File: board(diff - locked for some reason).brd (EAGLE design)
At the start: 161 x 100 mm, 19 parts, among them IC1 ATMEGA644-20PU, Q1 2N3906, T1 2N3904, T2 2N3904, T3 2N3904, T4 2N3904, U1 MCP1825S-3302E/DB

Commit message: modified board slightly
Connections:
- net GND: now also U1.2, U1.4
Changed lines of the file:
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@@
 <?xml version="1.0" encoding="utf-8"?>
 <!DOCTYPE eagle SYSTEM "eagle.dtd">
-<eagle version="8.4.0">
+<eagle version="8.4.1">
 <drawing>
 <settings>
@@
 <param name="dpMaxLengthDifference" value="10mm"/>
 <param name="dpGapFactor" value="2.5"/>
+<param name="checkAngle" value="0"/>
 <param name="checkFont" value="1"/>
 <param name="checkRestrict" value="1"/>
@@
 <contactref element="C2" pad="-"/>
 <contactref element="C1" pad="-"/>
-<wire x1="11.43" y1="12.05" x2="11.43" y2="20.94" width="0" layer="19" extent="1-1"/>
-<wire x1="29.75" y1="11.44" x2="11.43" y2="20.94" width="0" layer="19" extent="1-1"/>
-<wire x1="27.94" y1="80.01" x2="29.75" y2="11.44" width="0" layer="19" extent="1-1"/>
-<wire x1="16.51" y1="92.71" x2="29.75" y2="11.44" width="0" layer="19" extent="1-1"/>
+<contactref element="U1" pad="2"/>
+<contactref element="U1" pad="4"/>
+<wire x1="61.7996" y1="87" x2="68.2004" y2="87" width="0" layer="19" extent="1-1"/>
+<wire x1="27.94" y1="80.01" x2="61.7996" y2="87" width="0" layer="19" extent="1-1"/>
+<wire x1="16.51" y1="92.71" x2="27.94" y2="80.01" width="0" layer="19" extent="1-1"/>
 <wire x1="17.78" y1="62.23" x2="27.94" y2="80.01" width="0" layer="19" extent="1-1"/>
 <wire x1="17.78" y1="53.34" x2="17.78" y2="62.23" width="0" layer="19" extent="1-1"/>
 <wire x1="17.78" y1="44.45" x2="17.78" y2="53.34" width="0" layer="19" extent="1-1"/>
 <wire x1="17.78" y1="35.56" x2="17.78" y2="44.45" width="0" layer="19" extent="1-1"/>
+<wire x1="11.43" y1="20.94" x2="17.78" y2="35.56" width="0" layer="19" extent="1-1"/>
+<wire x1="11.43" y1="12.05" x2="11.43" y2="20.94" width="0" layer="19" extent="1-1"/>
+<wire x1="29.75" y1="11.44" x2="11.43" y2="12.05" width="0" layer="19" extent="1-1"/>
 </signal>
 <signal name="VCC">

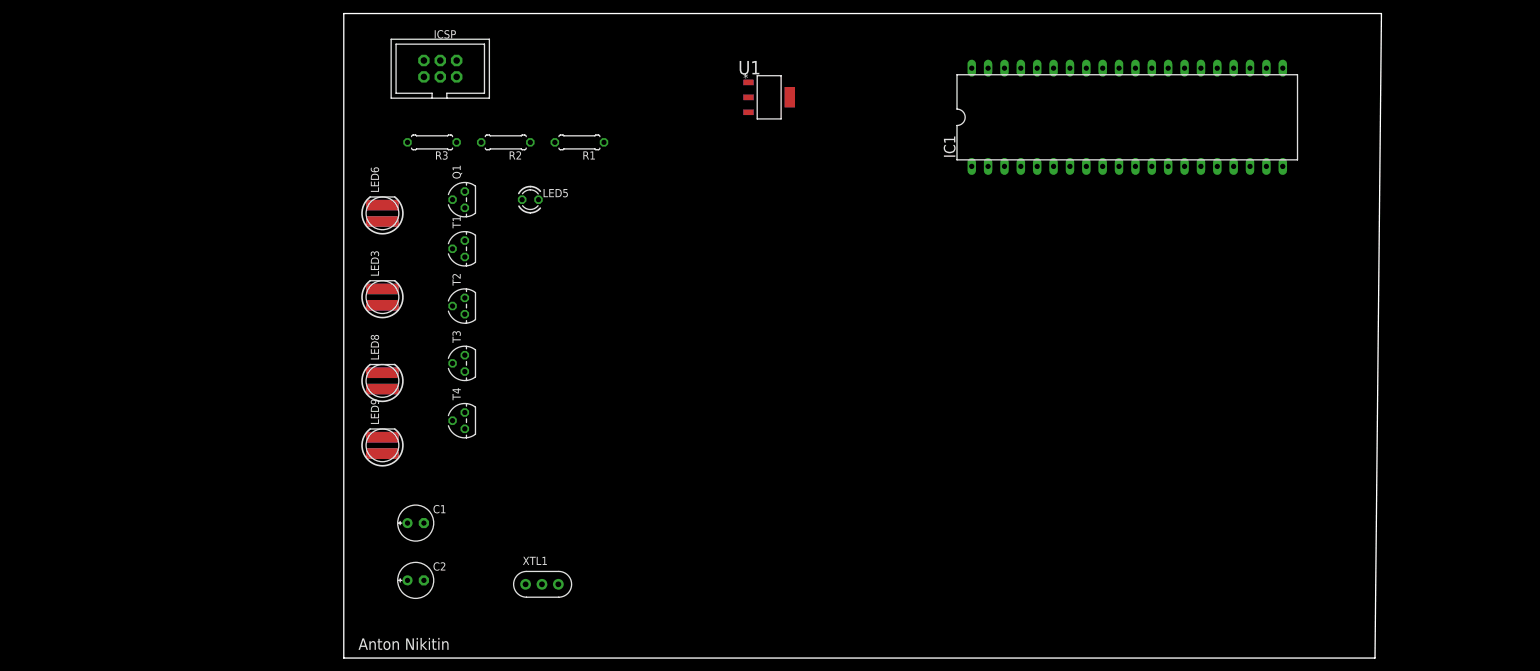
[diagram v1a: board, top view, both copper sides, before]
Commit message: added battery holders
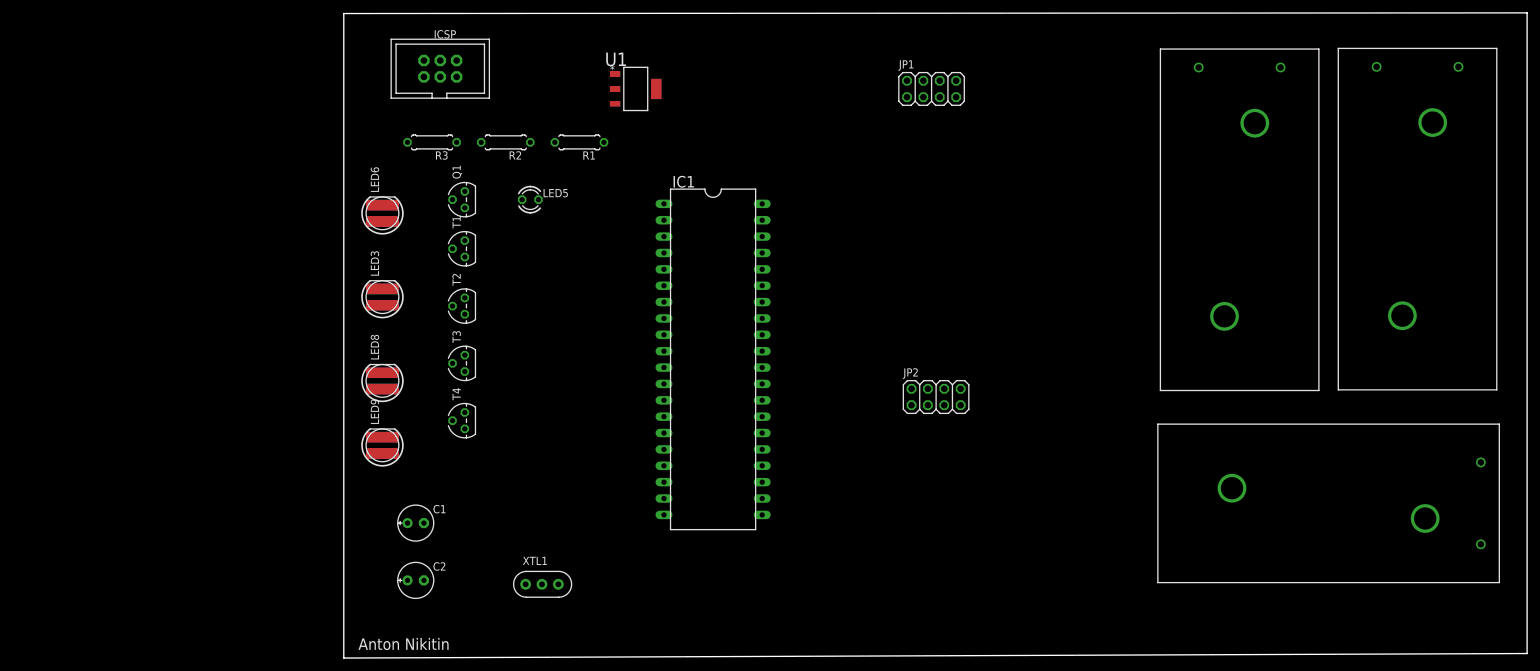
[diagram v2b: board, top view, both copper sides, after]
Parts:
- added J1, J2, J3: 2468, SamacSys_Parts:2468
- added JP1, JP2: (no value), pinhead:2X04
- moved IC1 74.4 mm to (56.3, 46.3), turned to 270 degrees
- moved U1 20.7 mm to (44.3, 88.3)
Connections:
- new net N$16: J1.1, J2.1, J3.1, U1.1
- net GND: now also J1.2, J2.2, J3.2
- net N$14: now also U1.3
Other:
- board size 161 x 100 mm -> 183.6 x 100.1 mm

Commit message: modified board to remove extra battery
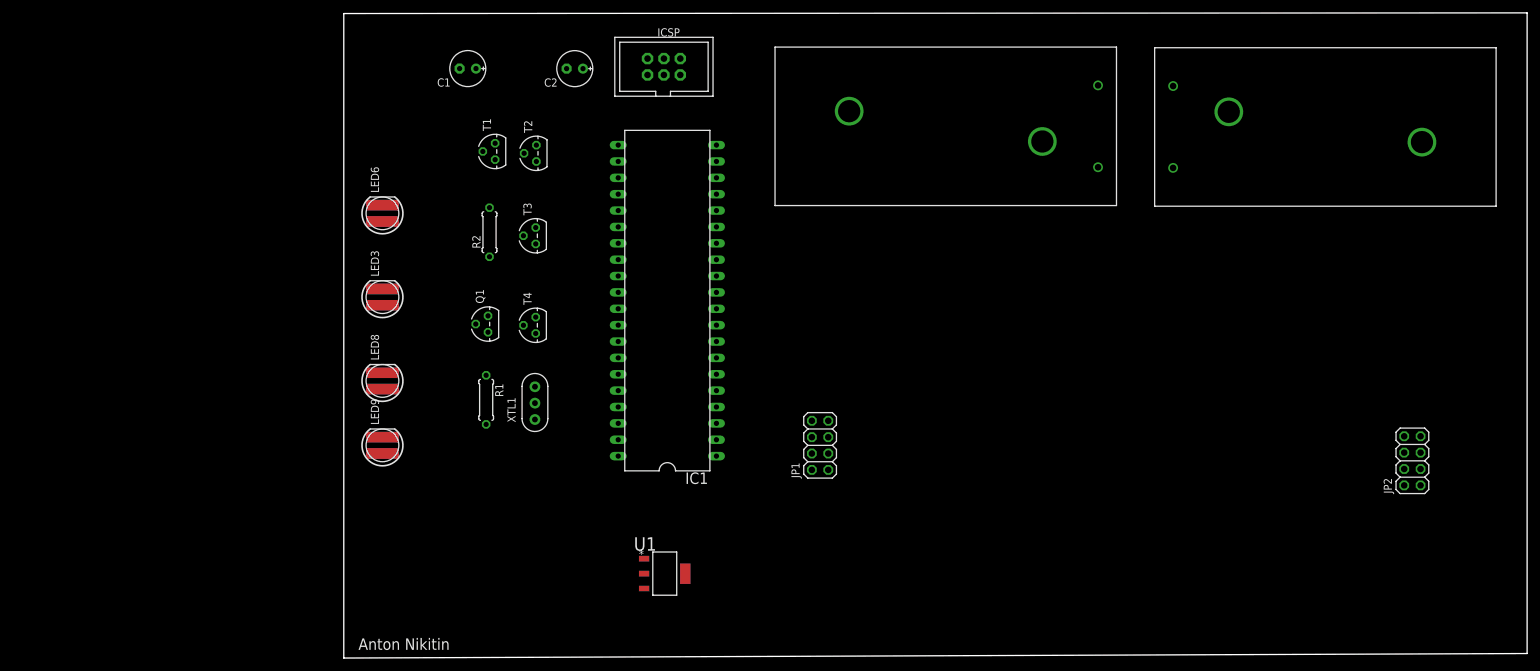
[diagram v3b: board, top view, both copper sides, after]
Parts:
- removed J1: 2468, SamacSys_Parts:2468
- removed LED5: (no value), led:LED3MM
- removed R3: 10K, resistor:0207/7
- moved C2 83.1 mm to (34.8, 91.5), turned to 180 degrees
- moved U1 75.3 mm to (48.8, 13.1)
- moved JP2 74.6 mm to (164.8, 30.6), turned to 90 degrees
- moved C1 71.0 mm to (18.2, 91.5), turned to 180 degrees
- moved J3 58.4 mm to (151.3, 82.4), turned to 180 degrees
- moved JP1 57.9 mm to (72.9, 33.0), turned to 90 degrees
- moved J2 47.8 mm to (92.4, 82.5), turned to 0 degrees
- moved R1 42.5 mm to (21.1, 40.1), turned to 270 degrees
- moved ICSP 34.7 mm to (48.7, 91.7)
- moved XTL1 28.1 mm to (28.7, 39.5), turned to 90 degrees
- moved T2 26.2 mm to (28.9, 78.3)
- moved T3 22.7 mm to (28.8, 65.5)
- moved Q1 19.6 mm to (21.4, 51.8)
- moved T4 18.4 mm to (28.8, 51.6)
- moved T1 15.8 mm to (22.5, 78.6)
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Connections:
- removed net N$13: IC1.9
- removed net N$6: LED5.K, R3.1
- removed net N$8: IC1.8, R3.2
- net GND: no longer J1.2
- net N$16: no longer J1.1
- net VCC: no longer LED5.A

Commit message: modified board
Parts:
- removed JP1, JP2: (no value), pinhead:2X04
- added SV1, SV2: (no value), con-lstb:MA05-2
- added U2: PEC11R-4015F-S0024, SamacSys_Parts:PEC12R-4XXXF-SXXXX_1
- moved J2 58.8 mm to (150.0, 70.5), flipped to the bottom
- moved J3 38.4 mm to (150.0, 44.0), flipped to the bottom, turned to 0 degrees
- moved U1 2.25 mm to (49.6, 15.2)
- moved T1 1.17 mm to (21.5, 78.0)
- moved T2 0.93 mm to (28.0, 78.0)
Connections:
- removed net N$7: Q1.2, R1.2
- new net N$21: IC1.21
- new net N$22: Q1.2, R1.1
- new net PA0: IC1.40, SV1.8
- new net PA1: IC1.39, SV1.6
- new net PA2: IC1.38, SV1.4
- new net PA3: IC1.37, SV1.2
- new net PA4: IC1.36, SV1.1
- new net PA5: IC1.35, SV1.3
- new net PA6: IC1.34, SV1.5
- new net PA7: IC1.33, SV1.7
- new net PC0: IC1.22, SV2.8
- new net PC1: IC1.23, SV2.6
- new net PC2: IC1.24, SV2.4
- new net PC3: IC1.25, SV2.2
- new net PC4: IC1.26, SV2.1
- new net PC5: IC1.27, SV2.3
- new net PC6: IC1.28, SV2.5
- new net PC7: IC1.29, SV2.7
- net GND: now also SV1.9, SV2.9
- net MOSI: now also R1.2; no longer R1.1
- net VCC: now also SV1.10, SV2.10
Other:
- board size 183.6 x 100.1 mm -> 183.6 x 100 mm

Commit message: modified board
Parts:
- R2: value 10K -> 10.0K
- moved R2 44.8 mm to (34.0, 23.0), turned to 180 degrees
- moved LED9 23.0 mm to (5.00, 10.0)
- moved LED6 21.0 mm to (5.00, 90.0)
- moved R1 17.3 mm to (24.0, 23.0), turned to 0 degrees
- moved XTL1 10.6 mm to (24.0, 30.0), turned to 180 degrees
- moved LED3 4.00 mm to (5.00, 60.0)
- moved U2 3.61 mm to (27.5, 12.4)
- moved LED8 3.00 mm to (5.00, 40.0)

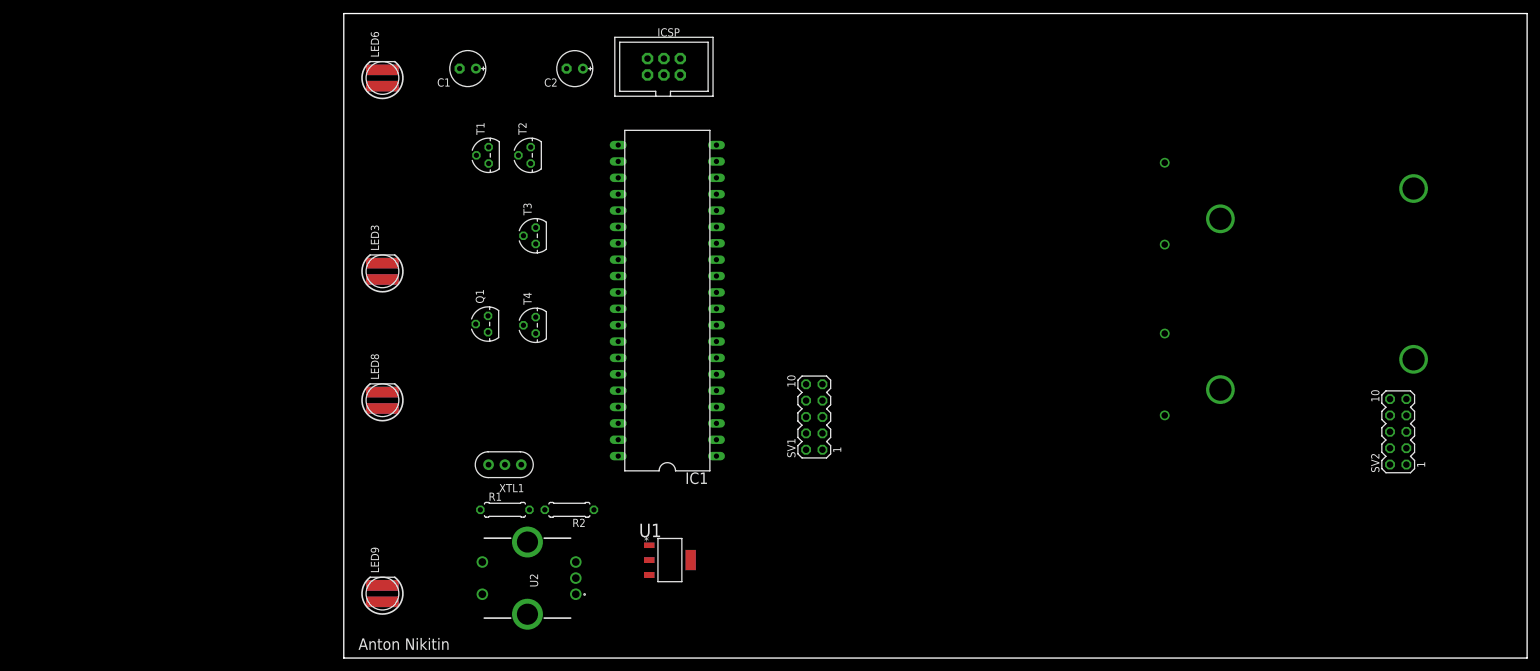
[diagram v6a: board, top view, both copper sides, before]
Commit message: modified board size
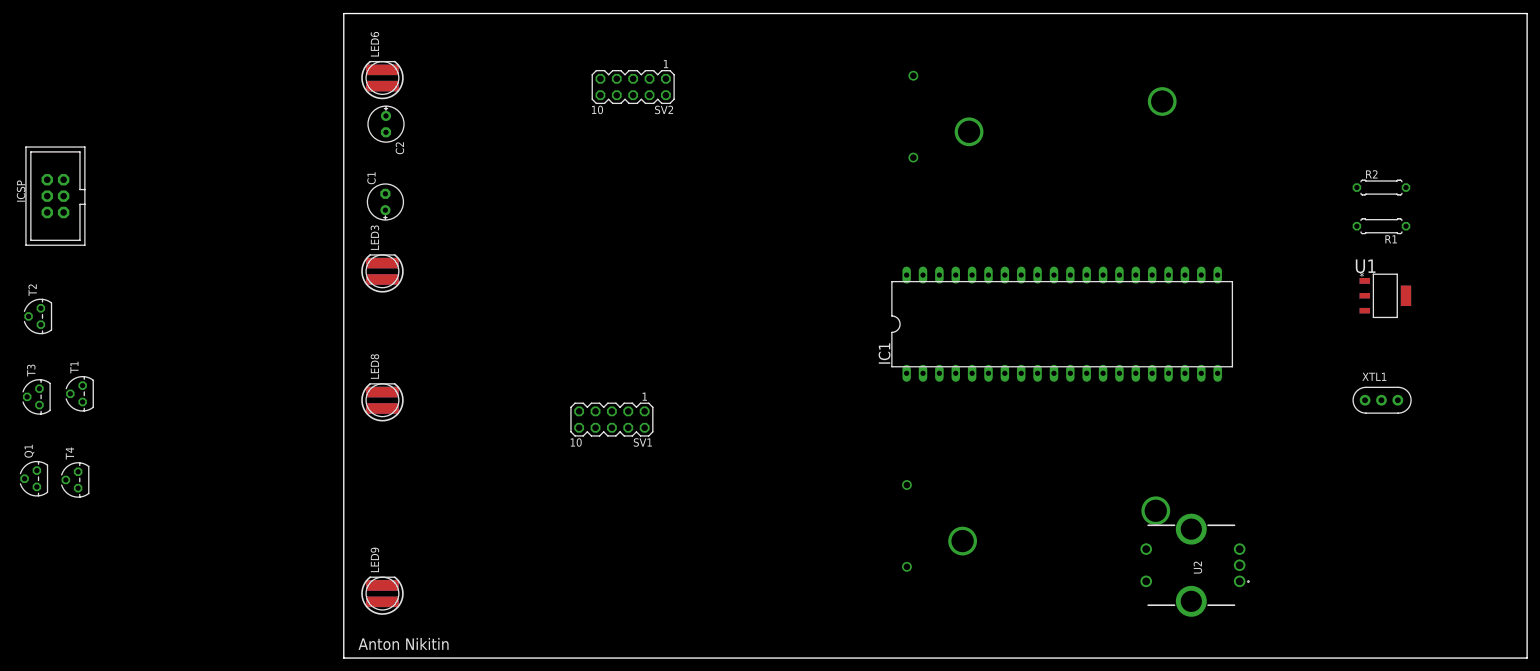
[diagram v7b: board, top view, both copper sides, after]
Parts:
- moved R1 142.9 mm to (160.0, 67.0), turned to 180 degrees
- moved XTL1 136.4 mm to (160.0, 40.0), turned to 0 degrees
- moved R2 135.6 mm to (160.0, 73.0), turned to 0 degrees
- moved SV2 130.2 mm to (43.9, 88.6), turned to 180 degrees
- moved U1 118.3 mm to (160.6, 56.2)
- moved U2 103.0 mm to (130.5, 14.4)
- moved ICSP 96.5 mm to (-45.7, 71.7), turned to 90 degrees
- moved T3 81.0 mm to (-48.2, 40.5)
- moved T2 80.0 mm to (-48.0, 53.0)
- moved T4 74.9 mm to (-42.2, 27.6)
- moved Q1 74.0 mm to (-48.6, 27.8)
- moved T1 73.1 mm to (-41.5, 41.0)
- moved J2 64.0 mm to (110.0, 20.5)
- moved IC1 61.4 mm to (110.5, 51.8), turned to 0 degrees
- moved J3 55.9 mm to (111.0, 84.0)
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
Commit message: finished connections on schematic
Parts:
- moved U2 110.0 mm to (20.5, 13.4)
- moved U1 107.0 mm to (55.0, 39.0)
- moved R1 106.2 mm to (55.0, 51.0)
- moved R2 106.2 mm to (55.0, 57.0)
- moved XTL1 106.2 mm to (55.0, 24.0)
- moved ICSP 100.9 mm to (55.0, 78.0), turned to 0 degrees
- moved Q1 67.0 mm to (18.4, 28.8)
- moved T1 67.0 mm to (25.5, 42.0)
- moved T2 67.0 mm to (19.0, 54.0)
- moved T3 67.0 mm to (18.8, 41.5)
- moved T4 67.0 mm to (24.8, 28.6)
- moved SV1 29.5 mm to (54.6, 11.0)
- moved SV2 25.5 mm to (54.9, 65.6)
- moved C1 22.4 mm to (26.8, 77.5), turned to 0 degrees
- moved LED6 16.0 mm to (5.00, 74.0)
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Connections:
- removed net N$12: IC1.11, IC1.31
- removed net N$14: IC1.10, IC1.30, U1.3
- new net N$13: IC1.16, U2.4
- new net N$6: IC1.14, U2.1
- new net N$7: IC1.15, U2.2
- new net N$8: IC1.10, IC1.30, IC1.32, U1.3, U2.3
- net N$21: now also IC1.1, IC1.11, IC1.18, IC1.19, IC1.2, IC1.20, IC1.3, IC1.31, IC1.4, IC1.5, U2.5
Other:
- board size 183.6 x 100 mm -> 140 x 87 mm
